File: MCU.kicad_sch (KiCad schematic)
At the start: 41 parts, among them IC9 ATSAMD21G18A-MF, J10 Conn_01x06, J7 Conn_01x08, J8 Conn_01x10, J9 Conn_01x08, Q1 XTAL_32.768KHZ_ABRACON_ABS09-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

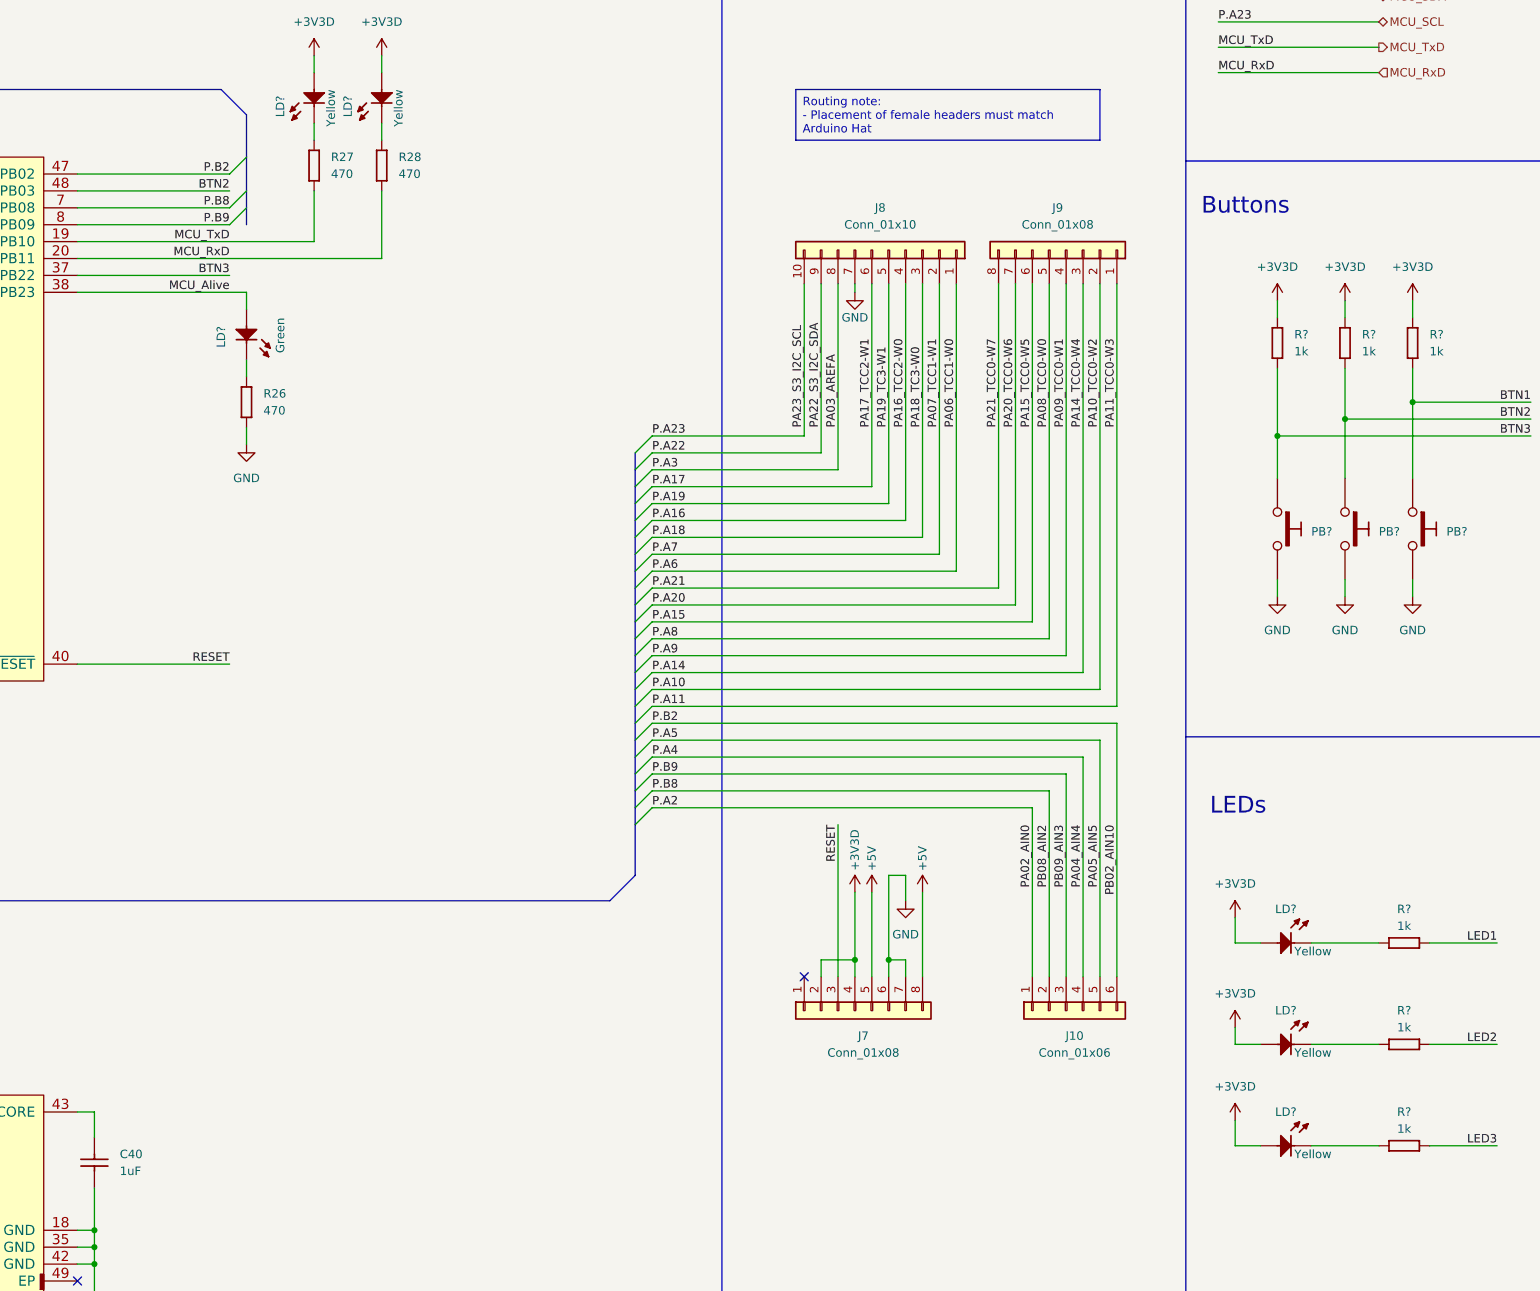
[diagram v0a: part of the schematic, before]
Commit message: Replaced buffers, added both bonded and packaged ACCURATE
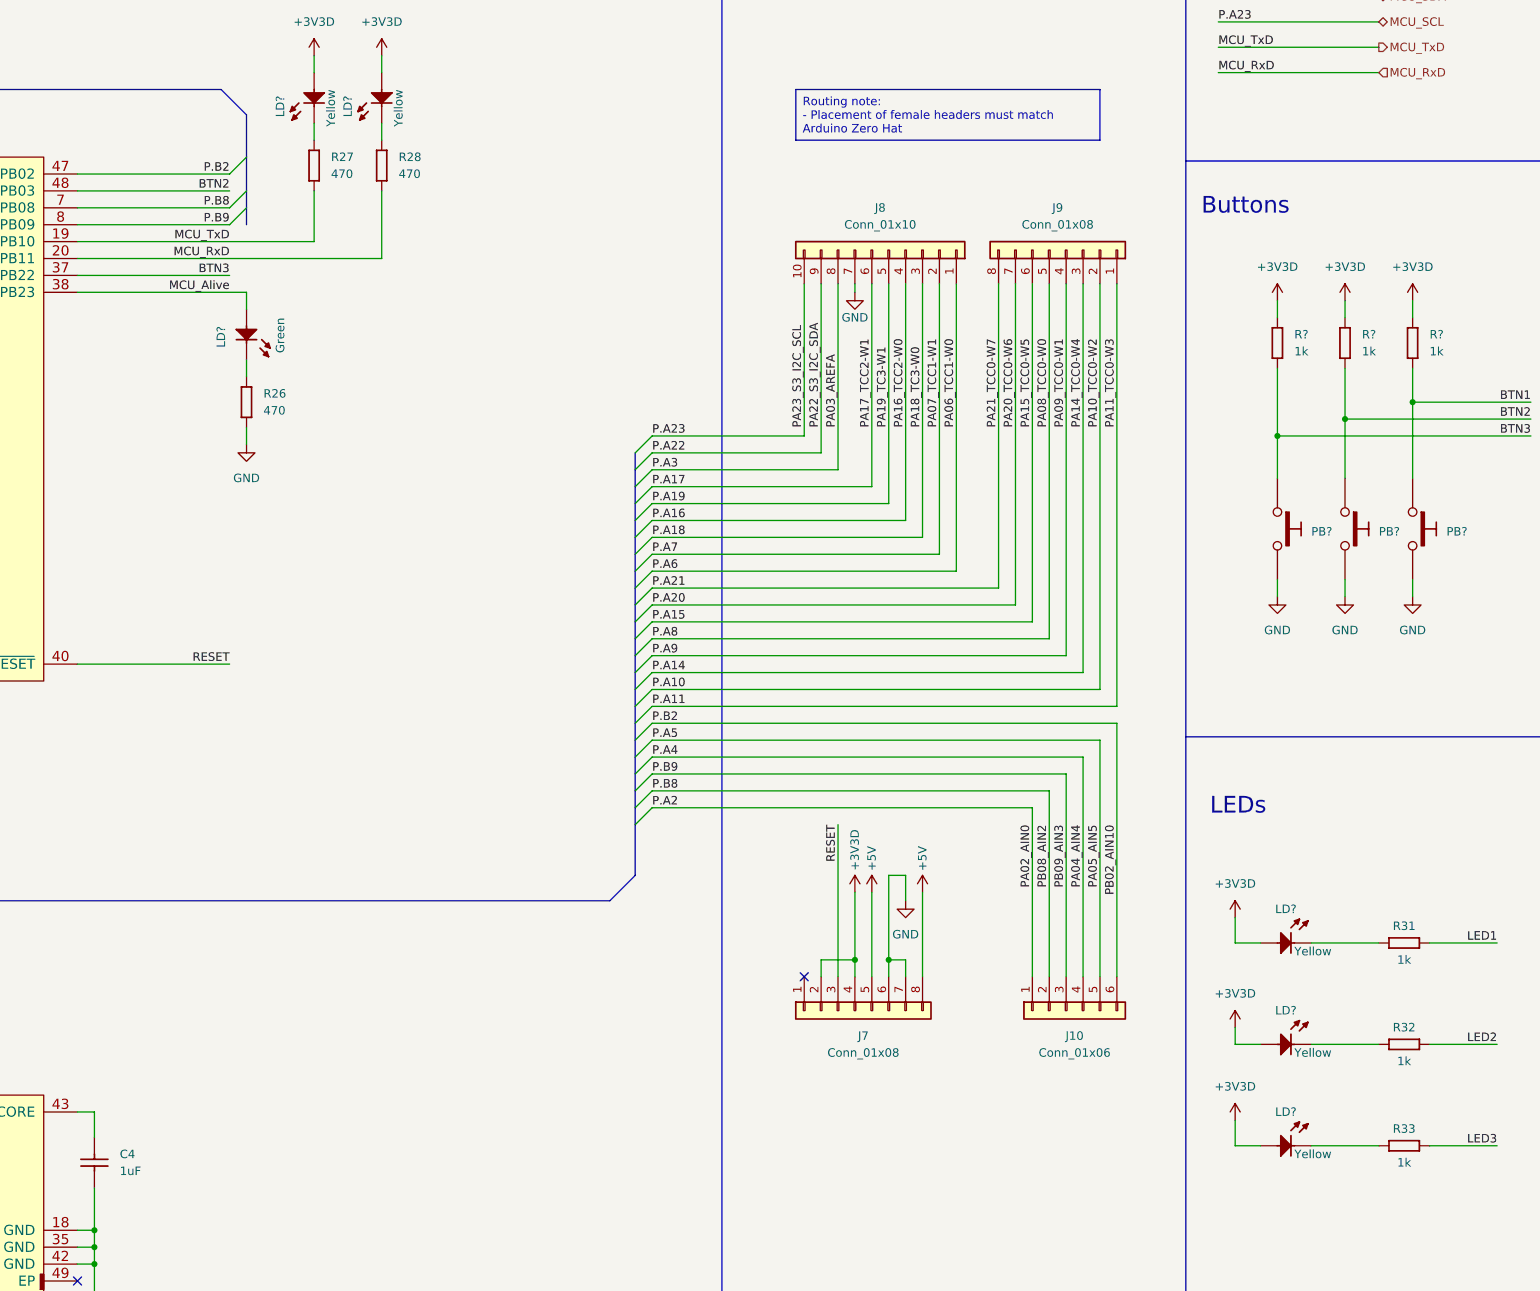
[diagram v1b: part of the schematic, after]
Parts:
- removed C40: CC0603_1UF_16V_10%_X7R, Capacitors SMD:CAPC1608X87N, symbol Capacitors SMD:CC0603_1UF_16V_10%_X7R
- removed R? (x3): R0603_1K0_0.1%_0.063W_10PPM, Resistors SMD:RESC1608X55N, symbol Resistors SMD:R0603_1K0_0.1%_0.063W_10PPM
- added C4: CC0603_1UF_25V_10%_X7R, Capacitors SMD:CAPC1608X87N, symbol Capacitors SMD:CC0603_1UF_25V_10%_X7R
- added R31, R32, R33: R0603_1K_1%_0.1W_100PPM, Resistors SMD:RESC1608X55N, symbol Resistors SMD:R0603_1K_1%_0.1W_100PPM
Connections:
- net GND: now also C4.2
- net LED1: now also R31.2
- net LED2: now also R32.2
- net LED3: now also R33.2
- net at LD?.1 (C): now also R31.1
- net at LD?.1 (C): now also R32.1
- net at LD?.1 (C): now also R33.1
- net at IC9.43 (VDDCORE): now also C4.1

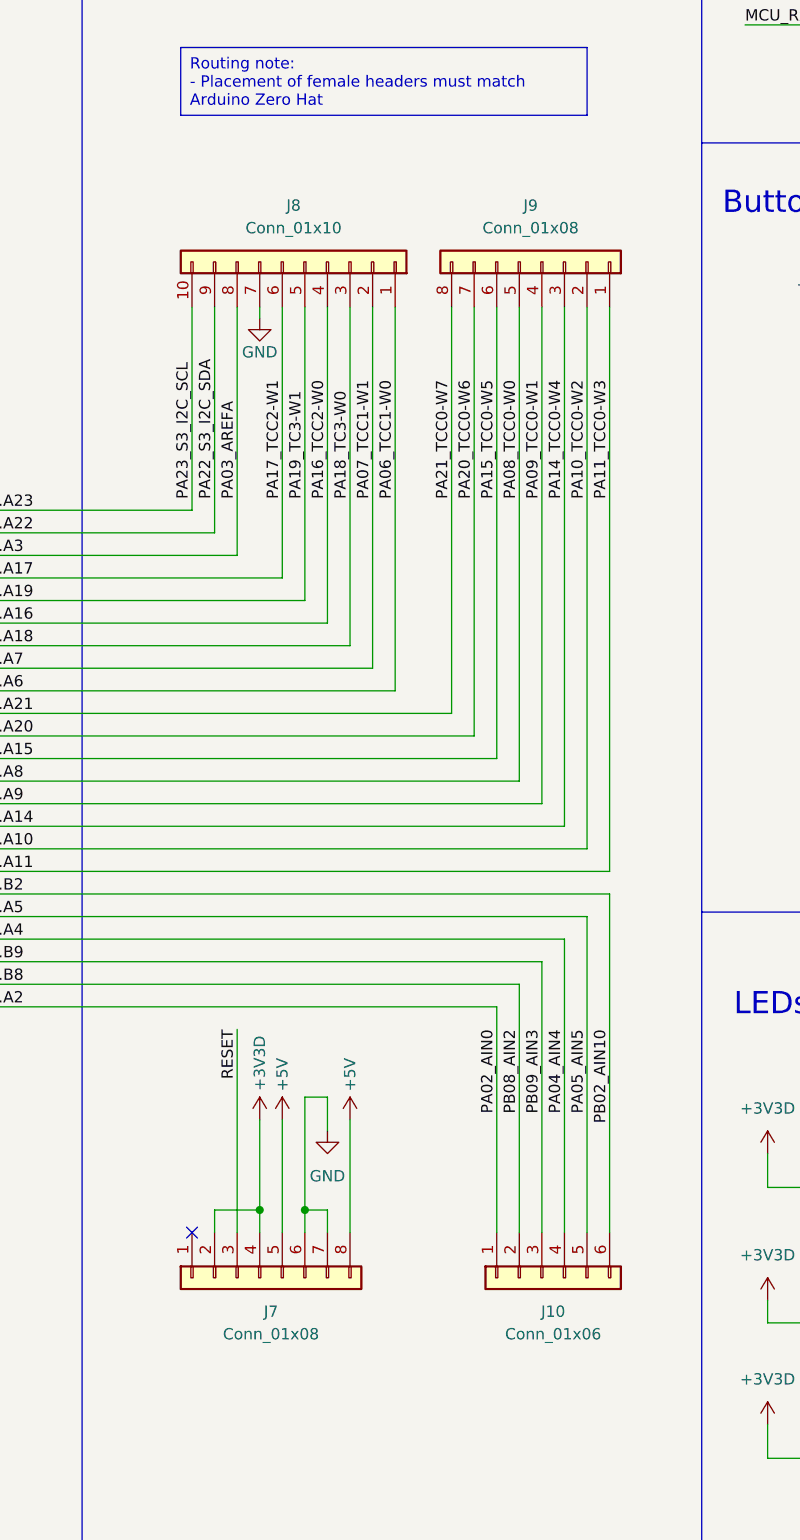
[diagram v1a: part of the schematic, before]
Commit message: Replaced the rest of the KiCADlib components with CERNlib ones
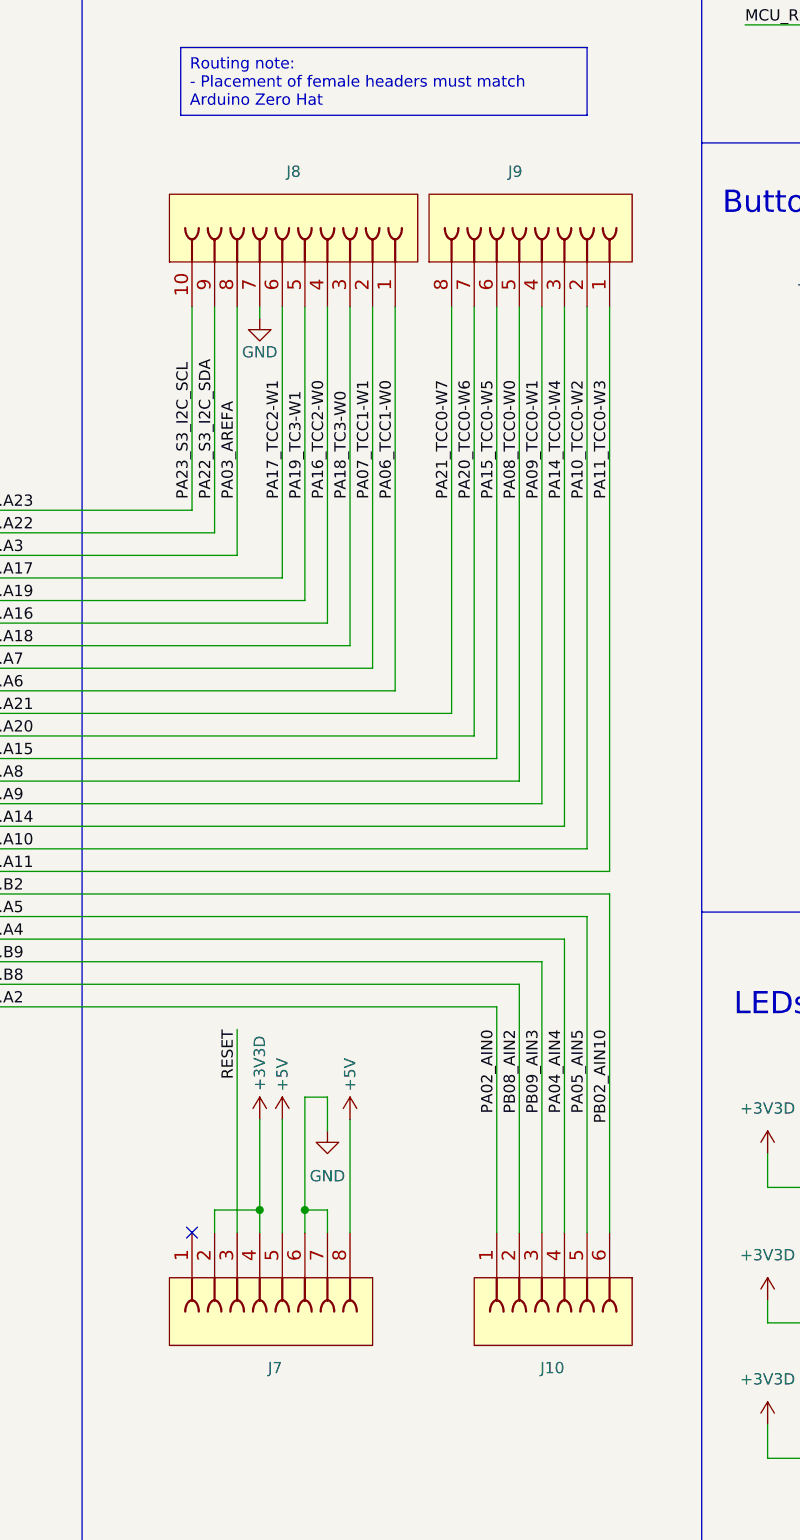
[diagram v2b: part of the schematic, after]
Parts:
- removed J10: Conn_01x06, Connector_PinSocket_2.54mm:PinSocket_1x06_P2.54mm_Vertical, symbol Connector_Generic:Conn_01x06
- removed J7, J9: Conn_01x08, Connector_PinSocket_2.54mm:PinSocket_1x08_P2.54mm_Vertical, symbol Connector_Generic:Conn_01x08
- removed J8: Conn_01x10, Connector_PinSocket_2.54mm:PinSocket_1x10_P2.54mm_Vertical, symbol Connector_Generic:Conn_01x10
- added J10: SAMTEC_SSW-106-01-L-S, SAMTEC THD:SAMTEC_SSW-106-01-L-S, symbol SAMTEC:SAMTEC_SSW-106-01-L-S
- added J7, J9: SAMTEC_SSW-108-01-G-S, SAMTEC THD:SAMTEC_SSW-108-01-G-S, symbol SAMTEC:SAMTEC_SSW-108-01-G-S
- added J8: SAMTEC_SSW-110-01-G-S, SAMTEC THD:SAMTEC_SSW-110-01-X-S, symbol SAMTEC:SAMTEC_SSW-110-01-G-S
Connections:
- net +3V3D: now also J7.2, J7.4
- net +5V: now also J7.5, J7.8
- net GND: now also J7.6, J7.7, J8.7
- net MCU_SCL: now also J8.10
- net MCU_SDA: now also J8.9
- net P.A10: now also J9.2
- net P.A11: now also J9.1
- net P.A14: now also J9.3
- net P.A15: now also J9.6
- net P.A16: now also J8.4
- net P.A17: now also J8.6
- net P.A18: now also J8.3
- net P.A19: now also J8.5
- net P.A2: now also J10.1
- net P.A20: now also J9.7
- net P.A21: now also J9.8
- net P.A3: now also J8.8
- net P.A4: now also J10.4
- net P.A5: now also J10.5
- net P.A6: now also J8.1
- net P.A7: now also J8.2
- net P.A8: now also J9.5
- net P.A9: now also J9.4
- net P.B2: now also J10.6
- net P.B8: now also J10.2
- net P.B9: now also J10.3
- net RESET: now also J7.3
